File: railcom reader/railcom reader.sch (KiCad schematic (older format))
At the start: 29 parts, among them J1 DCC_INPUT, J2 Signal output 1, U1 LM339, U2 L7805

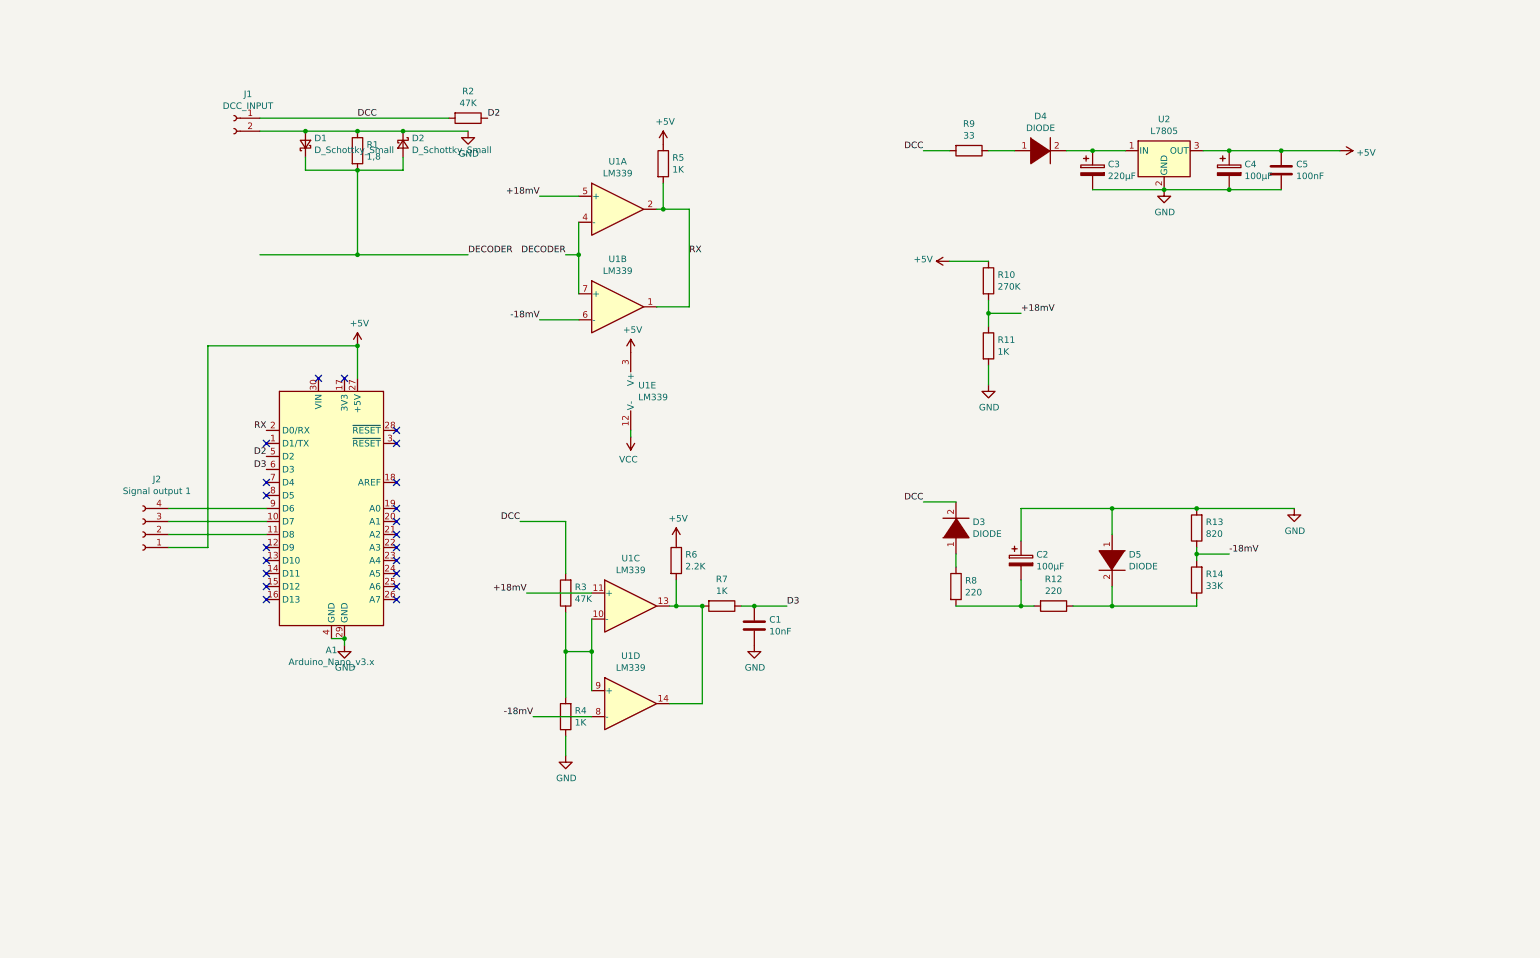
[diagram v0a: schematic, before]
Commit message: update schematic, netlist, pcb concept
modifications in comparing to railcom specification docs

original "splice" graphic found in topic was a bit confusing (imho)
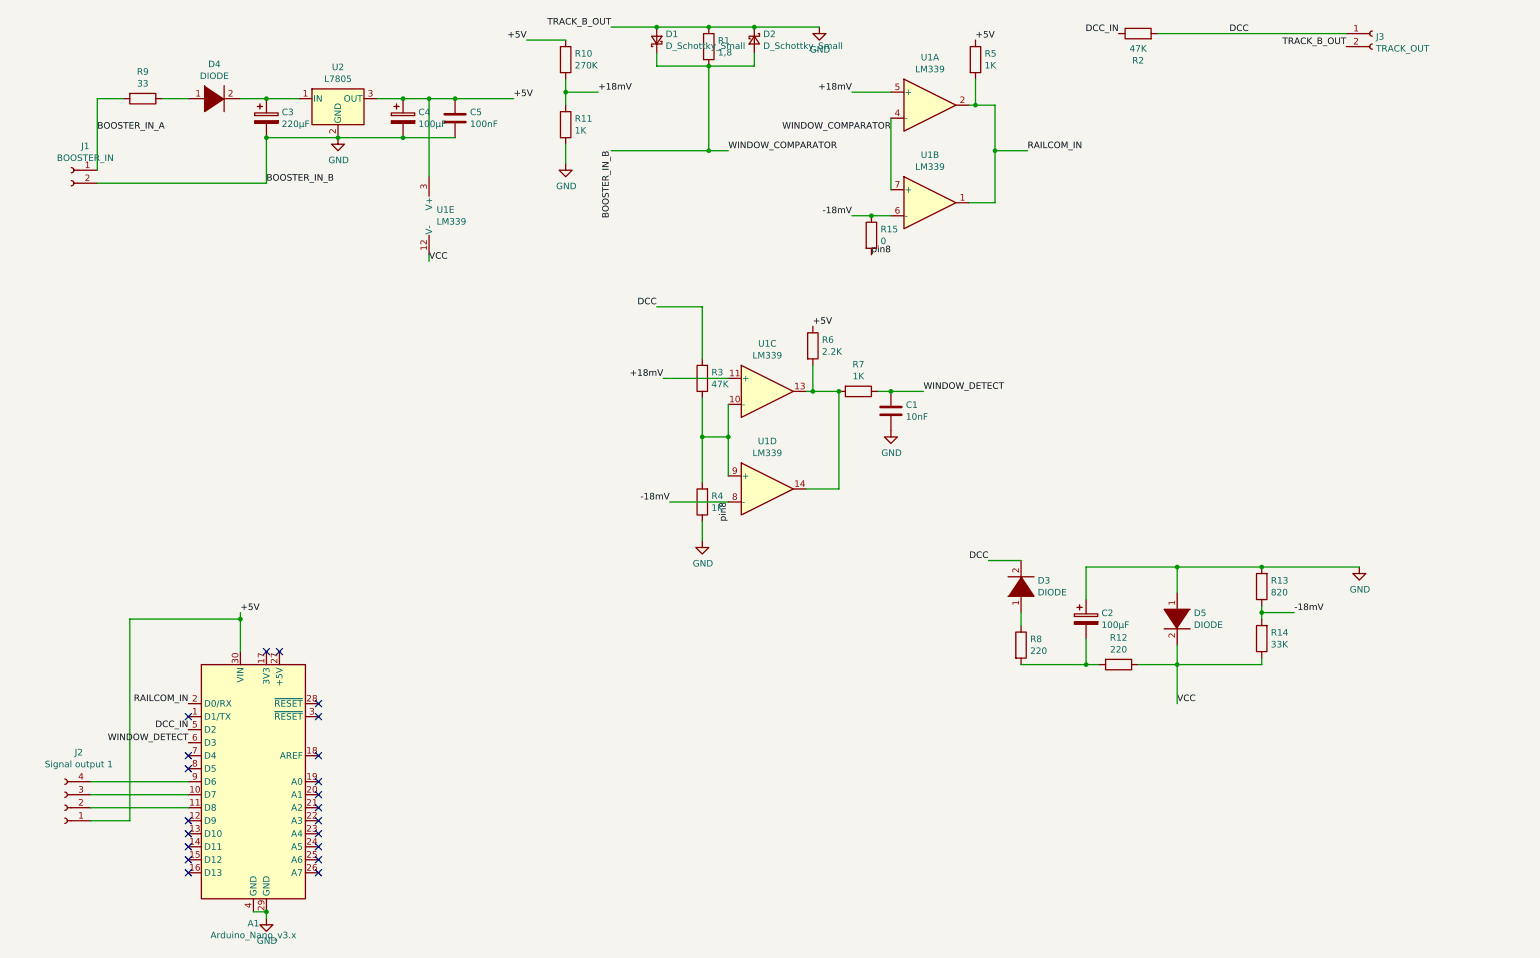
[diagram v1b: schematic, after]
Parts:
- added J3: TRACK_OUT, Connectors_Terminal_Blocks:TerminalBlock_Altech_AK300-2_P5.00mm, symbol Connector:Conn_01x02_Female
- added R15: 0, Resistors_THT:R_Axial_DIN0207_L6.3mm_D2.5mm_P7.62mm_Horizontal, symbol Device:R
- J1: value DCC_INPUT -> BOOSTER_IN
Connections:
- net DECODER is gone; now on net GND: D1.1 (K), D2.2 (A), R1.2, U1.4 (-), U1.7 (+)
- net +5V: now also A1.30 (VIN); no longer A1.27 (+5V)
- net -18mV: now also R15.1, R15.2
- net DCC: now also J3.1 (Pin_1); no longer J1.1 (Pin_1), R9.2
- net GND: now also J3.2 (Pin_2)
- net VCC: now also D5.2 (A), R12.1, R14.1
- net D2 renamed DCC_IN
- net D3 renamed WINDOW_DETECT
- net RX renamed RAILCOM_IN
- new net BOOSTER_IN_A: J1.1 (Pin_1), R9.2
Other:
- moved on the sheet: A1, C1, C2, C3, C4, C5, D1, D2, D3, D4, D5, J2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

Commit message: updated net labels & corrected some mistakes.
still getting 10 volts on the 7805. why though?
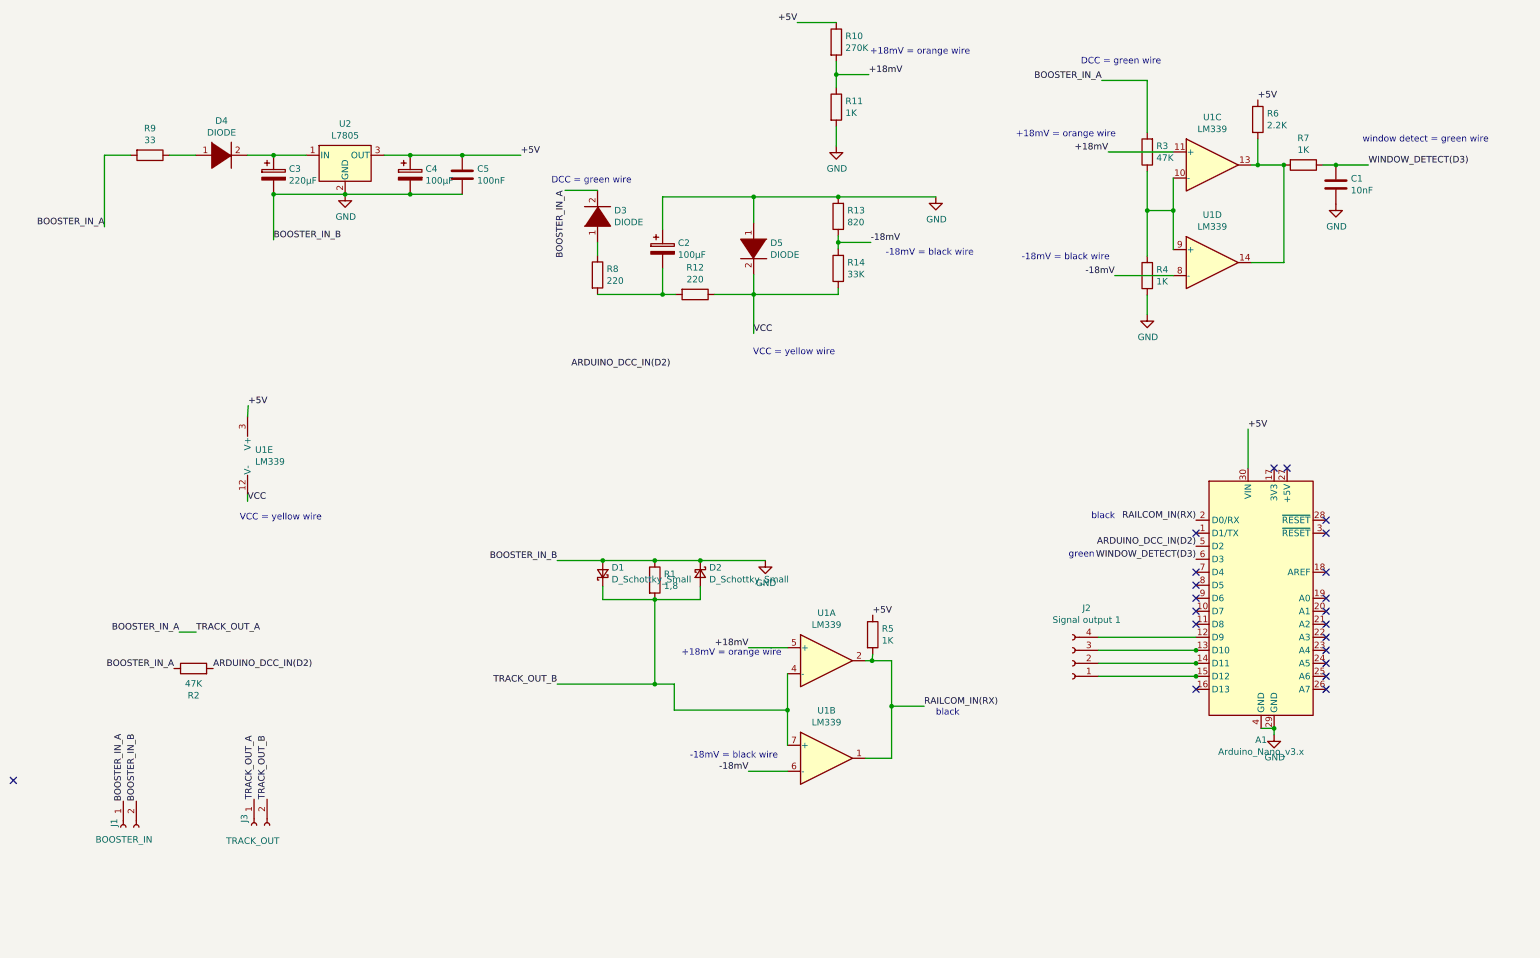
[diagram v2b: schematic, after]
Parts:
- removed R15: 0, Resistors_THT:R_Axial_DIN0207_L6.3mm_D2.5mm_P7.62mm_Horizontal, symbol Device:R
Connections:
- net labels added: ARDUINO_DCC_IN(D2), RAILCOM_IN(RX), TRACK_OUT_A, TRACK_OUT_B, WINDOW_DETECT(D3)
- net labels removed: DCC, DCC_IN, RAILCOM_IN, TRACK_B_OUT, WINDOW_COMPARATOR, WINDOW_DETECT, pin8
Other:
- note added: "+18mV = orange wire"
- note added: "-18mV = black wire"
- note added: "DCC = green wire\n"
- note added: "VCC = yellow wire\n"
- note added: "black"
- note added: "green\n"
- note added: "window detect = green wire\n"
- moved on the sheet: A1, C1, C2, C3, C4, C5, D1, D2, D3, D4, D5, J1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
